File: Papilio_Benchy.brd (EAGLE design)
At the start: 101.6 x 55.9 mm, 92 parts, among them SW1 EVQQ2, U1 93C46B, U2 LTC3419EMS, U3 FT2232D, U5 ARDUINO_MEGA_SHIELD, X1 6MHz

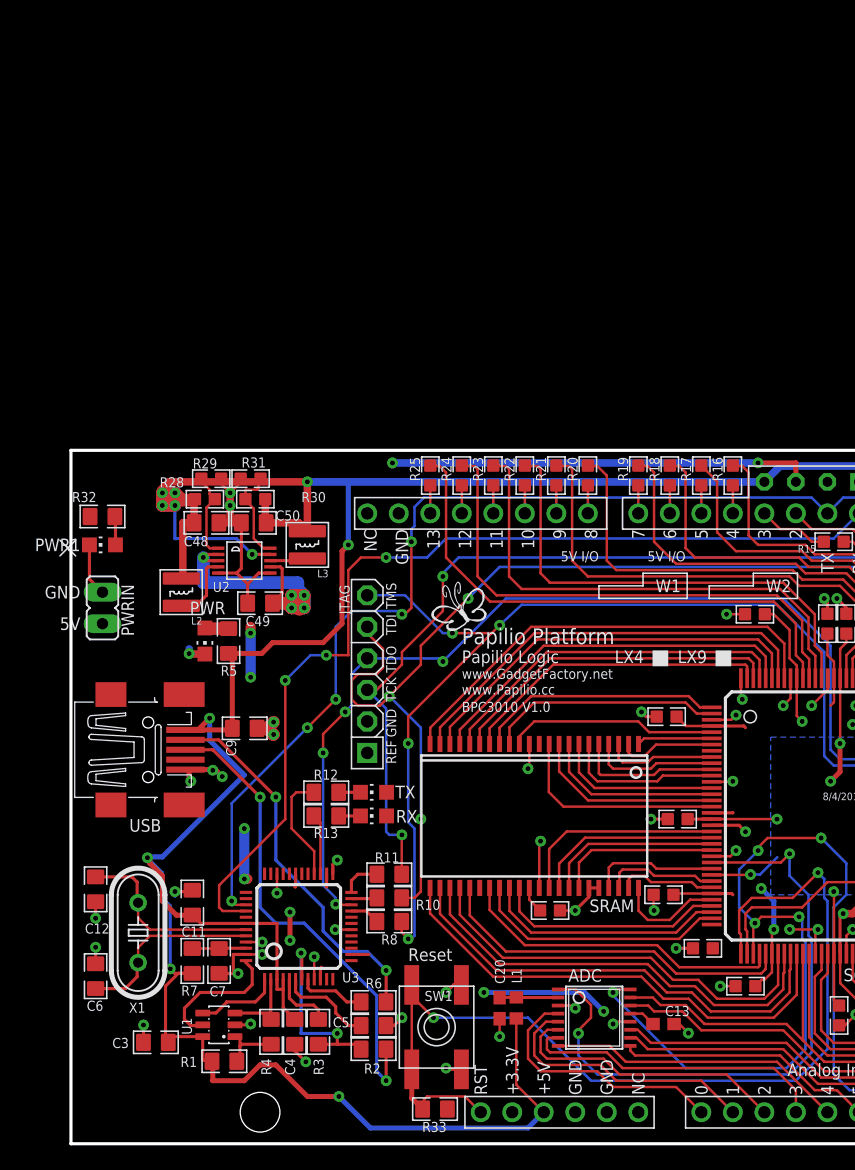
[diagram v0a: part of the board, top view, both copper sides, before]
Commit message: FT2232H upgrade
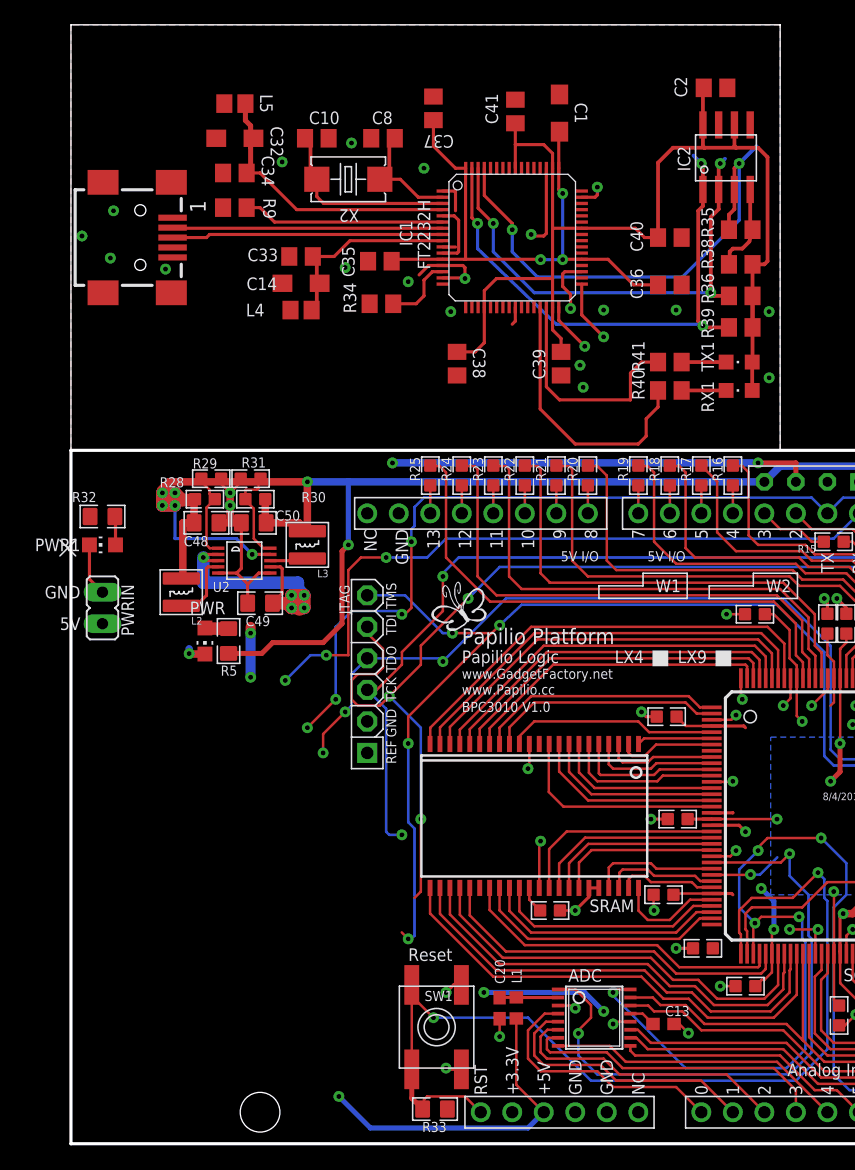
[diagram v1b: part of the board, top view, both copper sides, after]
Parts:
- removed C11, C3, C4, C5, C7, C9: 0.1uF, Bogdan_Commons:0805
- removed C12, C6: 27pF, Bogdan_Commons:0805
- removed R1: 10K, Bogdan_Commons:0805@1
- removed R10, R11, R8: 68, GadgetFactory:0805
- removed R12, R13: 220, GadgetFactory:0805
- removed R2, R6: 27R, Bogdan_Commons:0805@1
- removed R3: 1K5, Bogdan_Commons:0805@1
- removed R4: 2K2, Bogdan_Commons:0805@1
- removed R7: 470R, Bogdan_Commons:0805@1
- removed RX, TX: (no value), led:CHIP-LED0805
- removed U1: 93C46B, Bogdan_Commons:SOT23-6
- removed U3: FT2232D, Bogdan_Commons:LQFP48
- removed USB: MINI-USB-32005-201, con-cypressindustries:32005-201
- removed X1: 6MHz, crystal:HC49/S
- added C1: 3.3uF, dp_devices:SMC_A
- added C10, C8: 27pF, dp_devices:C805
- added C14, C32: 4.7uF, dp_devices:SMC_A
- added C2, C33, C34, C35, C36, C37, C38, C39, C40, C41: 0.1uF, dp_devices:C805
- added CONN1: CONN_USB, dp_devices:CONN_USB_MINI-B
- added IC1: FT2232H, DP-EagleLibrary:LQFP64
- added IC2: 93C46, dp_devices:SOIC8
- added L4, L5: (no value), dp_devices:FB805
- added R34, R36, R38, R39: 10k, dp_devices:R805
- added R35: 2.2k, dp_devices:R805
- added R40, R41: 470, dp_devices:R805
- added R9: 12k 1%, dp_devices:R805
- added RX1, TX1: (no value), dp_devices:LED-805
- added X2: 12MHz, dp_devices:4X6
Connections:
- removed net 3V3OUT_A: C5.2, U3.6
- removed net D+: R2.1, USB.3
- removed net D-: R6.1, USB.2
- removed net DO_A: R1.2, R4.1, U1.1
- removed net EECS_A: U1.5, U3.48
- removed net EEDATA_A: R4.2, U1.3, U3.2
- removed net EESK: U1.4, U3.1
- removed net FILTERED_VCC_A: C7.2, R7.1, U3.46
- removed net N$15_A: R3.2, U3.5
- removed net N$2: R12.2, RX.C
- removed net N$3: R13.2, TX.C
- removed net N$4: R13.1, U3.27
- removed net N$5: R12.1, U3.28
- removed net USBDM_A: R6.2, U3.8
- removed net USBDP_A: R2.2, R3.1, U3.7
- removed net USB_TCK: R11.1, U3.24
- removed net USB_TDI: R10.1, U3.23
- removed net USB_TMS: R8.1, U3.21
- removed net XTIN_A: C12.2, U3.43, X1.2
- removed net XTOUT_A: C6.2, U3.44, X1.1
- new net !PWEREN: IC1.60
- new net !RESET: IC1.14, R34.2
- new net !SUSPEND: IC1.36
- new net 1.8V: C1.+, C35.1, C36.1, C37.1, IC1.12, IC1.37, IC1.49, IC1.64
- new net 3.3V: C2.1, C38.1, C39.1, C40.1, C41.1, IC1.20, IC1.31, IC1.42, IC1.50, IC1.56, IC2.6, IC2.8, L4.2, L5.2, R34.1, R36.2, R38.2, R39.2, RX1.A, TX1.A
- new net AC0: IC1.26
- new net AC1: IC1.27
- new net AC2: IC1.28
- new net AC3: IC1.29, R40.1
- new net AC4: IC1.30, R41.1
- new net AC5: IC1.32
- new net AC6: IC1.33
- new net AC7: IC1.34
- new net AD0: IC1.16
- new net AD1: IC1.17
- new net AD2: IC1.18
- new net AD3: IC1.19
- new net AD4: IC1.21
- new net AD5: IC1.22
- new net AD6: IC1.23
- new net AD7: IC1.24
- new net BC0: IC1.48
- new net BC1: IC1.52
- new net BC2: IC1.53
- new net BC3: IC1.54
- new net BC4: IC1.55
- new net BC5: IC1.57
- new net BC6: IC1.58
- new net BC7: IC1.59
- new net BD0: IC1.38
- new net BD1: IC1.39
- new net BD2: IC1.40
- new net BD3: IC1.41
- new net BD4: IC1.43
- new net BD5: IC1.44
- new net BD6: IC1.45
- new net BD7: IC1.46
- new net DM: CONN1.D-, IC1.7
- new net DP: CONN1.D+, IC1.8
- new net EECLK: IC1.62, IC2.2, R36.1
- new net EECS: IC1.63, IC2.1, R39.1
- new net EEDATA: IC1.61, IC2.3, R35.2
- new net N$22: C8.1, IC1.2, X2.1
- new net N$23: C10.1, IC1.3, X2.2
- new net N$24: R40.2, RX1.C
- new net N$25: R41.2, TX1.C
- new net N$45: IC2.4, R35.1, R38.1
- new net N$48: C32.+, C34.1, IC1.4, L5.1
- new net N$49: C14.+, C33.1, IC1.9, L4.1
- new net N$9: IC1.6, R9.2
- net 3V3: no longer RX.A, TX.A, U3.10, U3.14, U3.26, U3.31
- net 5V: now also CONN1.VUSB
- net 5V0: no longer C11.2, C3.2, C4.2, C9.2, R1.1, R7.2, U1.6, U3.3, U3.4, U3.42, USB.1
- net GND: now also C1.-, C10.2, C14.-, C2.2, C32.-, C33.2, C34.2, C35.2, C36.2, C37.2, C38.2, C39.2, C40.2, C41.2, C8.2, CONN1.GND, IC1.1, IC1.10, IC1.11, IC1.13, IC1.15, IC1.25, IC1.35, IC1.47, IC1.5, IC1.51, IC2.5, R9.1; no longer C11.1, C12.1, C3.1, C4.1, C5.1, C6.1, C7.1, C9.1, U1.2, U3.18, U3.25, U3.34, U3.45, U3.47, U3.9, USB.5
- net TCK: no longer R11.2
- net TDI: no longer R10.2
- net TDO: no longer U3.22
- net TMS: no longer R8.2
- net USB_RXD: no longer U3.39
- net USB_TXD: no longer U3.40
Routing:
- net 3.3V: track 0.00 -> 89.5 mm
- net 5V0: track 288.6 -> 199.1 mm, vias 7 -> 4
- net 1.8V: track 0.00 -> 45.6 mm, vias 0 -> 3
- net EECS: track 0.00 -> 43.8 mm, vias 0 -> 3
- net EEDATA: track 0.00 -> 40.9 mm, vias 0 -> 2
- net EECLK: track 0.00 -> 39.0 mm, vias 0 -> 3
- net D+: track 38.5 -> 0.00 mm, vias 2 -> 0
- net D-: track 30.5 -> 0.00 mm, vias 2 -> 0
- net N$48: track 0.00 -> 24.7 mm
- net USB_TXD: track 88.9 -> 66.1 mm
- net AC3: track 0.00 -> 22.3 mm
- net DP: track 0.00 -> 21.9 mm
- net DM: track 0.00 -> 21.8 mm
- net AC4: track 0.00 -> 18.4 mm
- net USB_RXD: track 82.9 -> 65.1 mm, vias 6 -> 5
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- added copper zone on layer 1, net GND
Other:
- board size 101.6 x 55.9 mm -> 101.6 x 90.2 mm
- board text added: "!PWEREN"
- board text added: "!RESET"
- board text added: "1.8V"
- board text added: "3V3"
- board text added: "ACBUS0"
- board text added: "ACBUS1"
- board text added: "ACBUS2"
- board text added: "ACBUS3"
- board text added: "ACBUS4"
- board text added: "ACBUS5"
- board text added: "ACBUS6"
- board text added: "ACBUS7"
- board text added: "ADBUS0"
- board text added: "ADBUS1"
- board text added: "ADBUS2"
- board text added: "ADBUS3"
- board text added: "ADBUS4"
- board text added: "ADBUS5"
- board text added: "ADBUS6"
- board text added: "ADBUS7"
- board text added: "BCBUS0"
- board text added: "BCBUS1"
- board text added: "BCBUS2"
- board text added: "BCBUS3"
- board text added: "BCBUS4"
- board text added: "BCBUS5"
- board text added: "BCBUS6"
- board text added: "BCBUS7"
- board text added: "BDBUS0"
- board text added: "BDBUS1"
- board text added: "BDBUS2"
- board text added: "BDBUS3"
- board text added: "BDBUS4"
- board text added: "BDBUS5"
- board text added: "BDBUS6"
- board text added: "BDBUS7"
- board text added: "Dangerous Prototypes"
- board text added: "EECLK"
- board text added: "EECS"
- board text added: "EEDATA"
- board text added: "FT2232H Breakout Board v1a"
- board text added: "Fulfillment By:"
- board text added: "Seeed Studio"
- board text added: "dangerousprototypes.com"
- board text added: "seeedstudio.com"

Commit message: Arduino Leonardo
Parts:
- added C11, C9: 22p, SmartPrj:C0603-ROUND
- added C3, C4, C6: 100n, SmartPrj:C0603-ROUND
- added C5, C7: 1uF, SmartPrj:C0603-ROUND
- added D2: CD1206-S01575, diode:MINIMELF
- added J1: USB MICRO, SmartPrj:CON2_USB_MICRO_B_AT
- added L, RX, TX: Yellow, led:CHIPLED_0805
- added L6: MH2029-300Y, wuerth-elektronik:0805
- added ON: Green, led:CHIPLED_0805
- added R1: 1M, SmartPrj:R0603-ROUND
- added R2, R3: NM, SmartPrj:R0402
- added R4, R6: 22R, GadgetFactory_6.0:0805
- added R7, R8: 10K, GadgetFactory_6.0:0805
- added RN2: 1K, resistor-dil:CAY16
- added U1: ATMEGA32U4-XUMU, SmartPrj:QFN44ML7X7
- added U3: ATMEGA32U4-XUAU, SmartPrj:TQFP44-PAD
- added Y1: 16MHz KX-7, SmartPrj:CRYSTAL-3.2-2.5
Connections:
- new net +5V: C3.1, C4.1, D2.C, L6.1, R7.2, RN2.1, RN2.3, RN2.4, U1.14, U1.2, U1.34, U3.14, U3.2, U3.34
- new net AGND: C6.1, R2.1, U1.43, U3.43
- new net AREF: C6.2, U1.42, U3.42
- new net AVCC: C5.1, L6.2, U1.24, U1.44, U3.24, U3.44
- new net D+: J1.P3, R6.1
- new net D-: J1.P2, R4.1
- new net D0/RX: U1.20, U3.20
- new net D1/TX: U1.21, U3.21
- new net D2/SDA: U1.19, U3.19
- new net D3/SCL: U1.18, U3.18
- new net D5*: U1.31, U3.31
- new net D6*: U1.27, U3.27
- new net HWB: R8.2, U1.33, U3.33
- new net IO10*: U1.30, U3.30
- new net IO11*: U1.12, U3.12
- new net IO12: U1.26, U3.26
- new net IO13*: RN2.2, U1.32, U3.32
- new net IO8: U1.28, U3.28
- new net IO9*: U1.29, U3.29
- new net MISO: U1.11, U3.11
- new net MOSI: U1.10, U3.10
- new net N$2: L.A, RN2.7
- new net N$3: ON.A, RN2.8
- new net N$4: RN2.6, TX.A
- new net N$5: RN2.5, RX.A
- new net RD+: R6.2, U1.4, U3.4
- new net RD-: R4.2, U1.3, U3.3
- new net RXLED: RX.C, U1.8, U3.8
- new net SCK: U1.9, U3.9
- new net TXLED: TX.C, U1.22, U3.22
- new net UCAP: C7.1, U1.6, U3.6
- new net UGND: C7.2, R3.2, U1.5, U3.5
- new net USBID: J1.P4
- new net VUSB: U1.7, U3.7
- new net XTAL1: C11.1, R1.1, U1.17, U3.17, Y1.1
- new net XTAL2: C9.2, R1.2, U1.16, U3.16, Y1.3
- new net XUSB: J1.P1
- net A0: now also U1.36, U3.36
- net A1: now also U1.37, U3.37
- net A2: now also U1.38, U3.38
- net A3: now also U1.39, U3.39
- net A4: now also U1.40, U3.40
- net A5: now also U1.41, U3.41
- net D4: now also U1.25, U3.25
- net D7: now also U1.1, U3.1
- net GND: now also C11.2, C3.2, C4.2, C5.2, C9.1, J1.P5, J1.S1, J1.S2, J1.S3, J1.S4, J1.S5, J1.S6, L.C, ON.C, R2.2, R3.1, R8.1, U1.15, U1.23, U1.35, U1.EXP, U3.15, U3.23, U3.35, U3.P$1, Y1.2, Y1.4
- net RESET: now also D2.A, R7.1, U1.13, U3.13
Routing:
- net GND: track 147.1 -> 188.1 mm, vias 68 -> 78
- net +5V: track 0.00 -> 20.8 mm, vias 0 -> 1
- net UGND: track 0.00 -> 13.7 mm, vias 0 -> 1
- net XTAL1: track 0.00 -> 13.4 mm
- net RESET: track 80.7 -> 94.0 mm
- net N$3: track 0.00 -> 12.5 mm
- net AREF: track 0.00 -> 12.2 mm
- net XTAL2: track 0.00 -> 10.4 mm
- net N$2: track 0.00 -> 9.32 mm
- net N$5: track 0.00 -> 7.35 mm
- net N$4: track 0.00 -> 6.98 mm
- net AGND: track 0.00 -> 6.81 mm, vias 0 -> 1
- net UCAP: track 0.00 -> 6.00 mm
- net AVCC: track 0.00 -> 5.77 mm
- net D+: track 0.00 -> 3.87 mm
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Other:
- board text added: "ITALY"
- board text added: "MADE IN"
- board text added: "X2"
